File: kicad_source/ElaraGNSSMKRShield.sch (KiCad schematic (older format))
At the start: 37 parts, among them CN1 ARDUINO_MKR, CN2 60312202114509, Q1 BSS138, Q2 BSS138, U1 TPS736XX, U2 WIRL-POSI_Elara-I, U3 PCA9306, U4 SN74LVC2G34

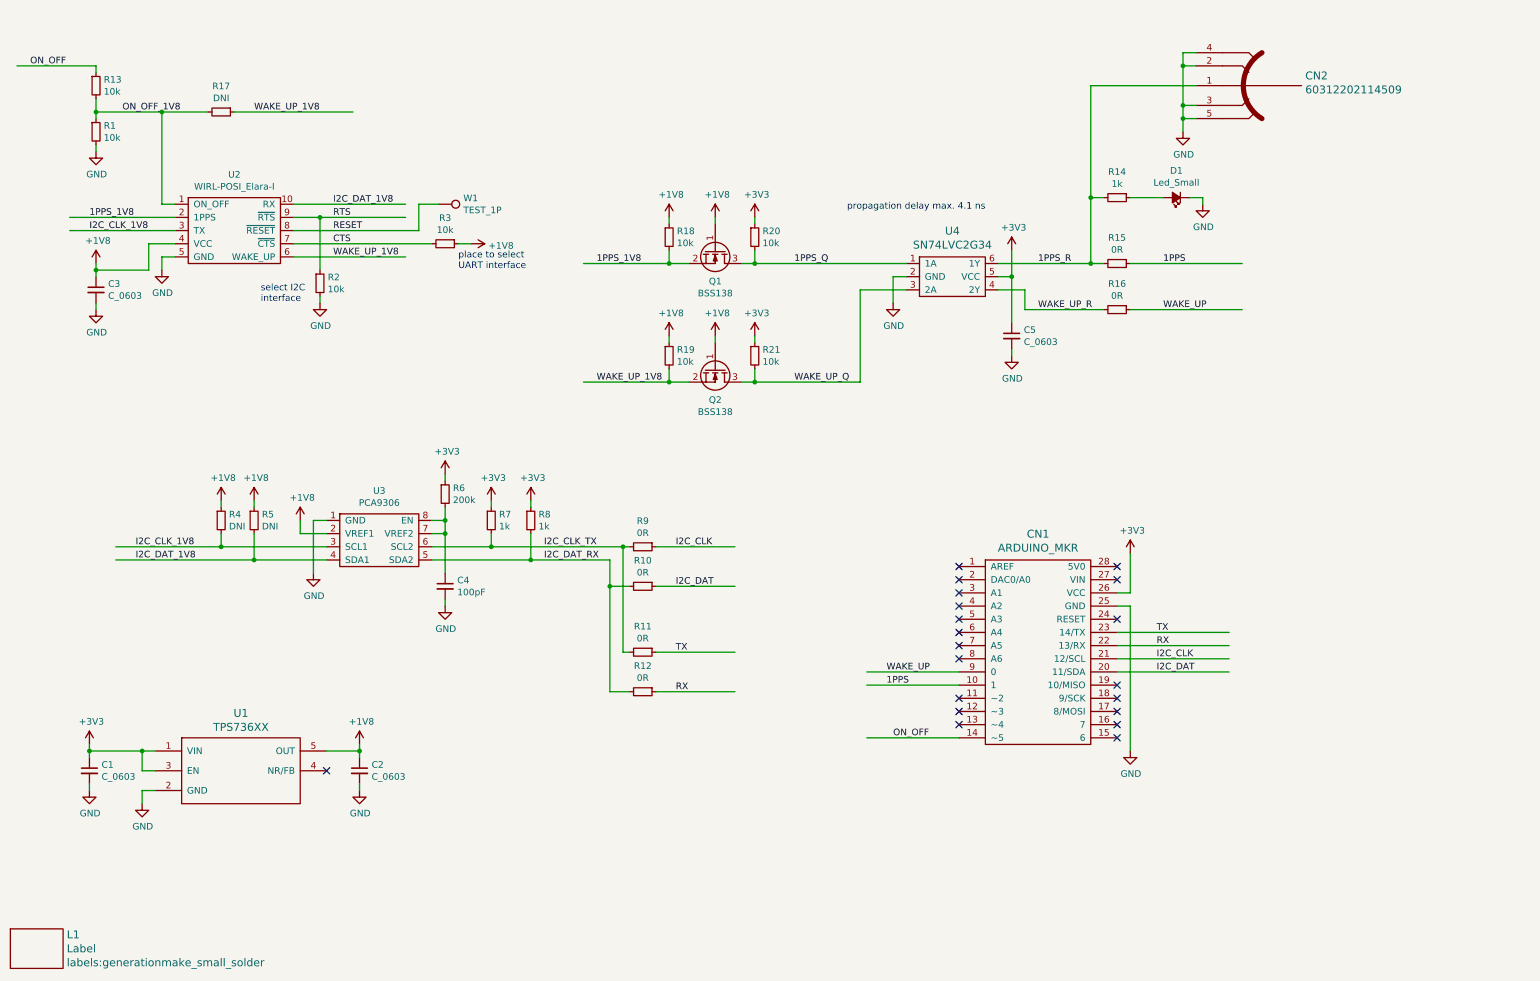
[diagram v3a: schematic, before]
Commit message: added wuerth part numbers
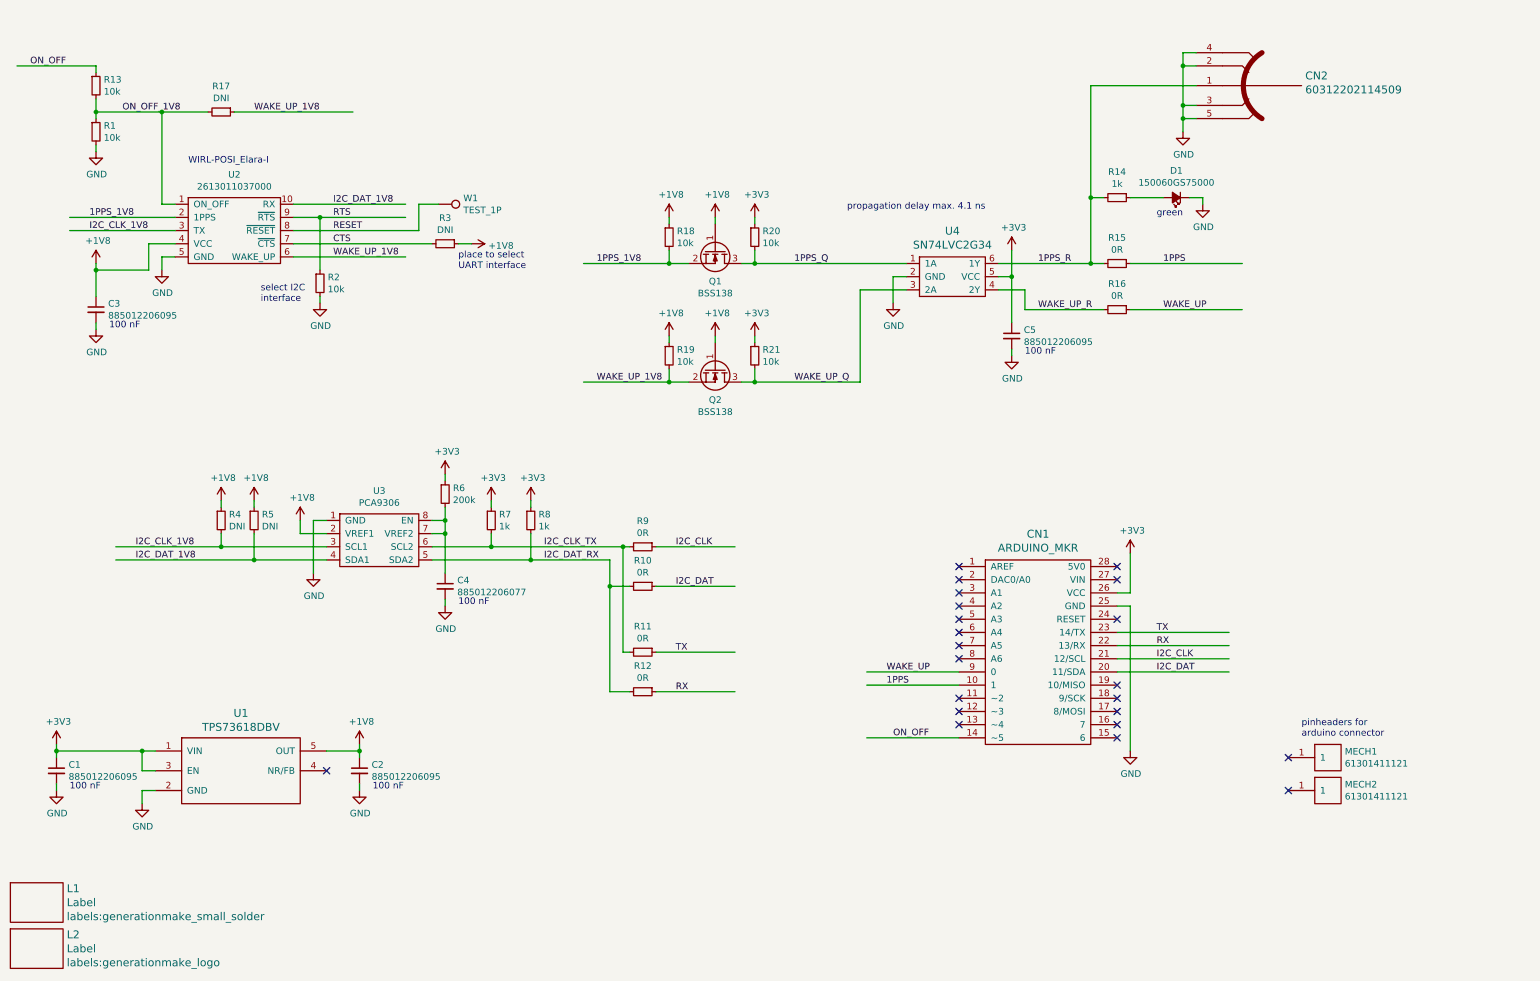
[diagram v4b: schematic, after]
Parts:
- added L2: Label, labels:generationmake_logo, symbol devices:Label
- added MECH1, MECH2: 61301411121, symbol MECH_mounting-holes:MHNP_2.1_4.0
- C1, C2, C3, C5: value C_0603 -> 885012206095
- C4: value 100pF -> 885012206077
- D1: value Led_Small -> 150060GS75000
- R3: value 10k -> DNI
- U1: value TPS736XX -> TPS73618DBV
- U2: value WIRL-POSI_Elara-I -> 2613011037000
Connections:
- no-connect marks 20 -> 22
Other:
- note added: "100 nF"
- note added: "WIRL-POSI_Elara-I"
- note added: "green"
- note added: "pinheaders for\narduino connector"
- moved on the sheet: C1, C3, L1
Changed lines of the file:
@@
 Sheet 1 1
 Title "ElaraGNSSMKRShield"
-Date "2020-11-16"
+Date "2020-12-22"
 Rev "0.1"
 Comp "generationmake"
@@
 P 2200 2150
 F 0 "U2" H 2200 2575 50  0000 C CNN
-F 1 "WIRL-POSI_Elara-I" H 2200 2484 50  0000 C CNN
+F 1 "2613011037000" H 2200 2484 50  0000 C CNN
 F 2 "RF_GPS:wuerth_WIRL-POSI_Elara-I" H 2200 2150 50  0001 C CNN
 F 3 "" H 2200 2150 50  0001 C CNN
@@
 P 2250 6200
 F 0 "U1" H 2250 6587 60  0000 C CNN
-F 1 "TPS736XX" H 2250 6481 60  0000 C CNN
+F 1 "TPS73618DBV" H 2250 6481 60  0000 C CNN
 F 2 "SOT_TO:SOT-23-5" H 2250 6350 60  0001 C CNN
 F 3 "" H 2250 6200 60  0000 C CNN
@@
 L power-supply:+3V3 #PWR01
 U 1 1 5F8A3C41
-P 1100 6050
-F 0 "#PWR01" H 1100 5900 50  0001 C CNN
-F 1 "+3V3" H 1115 6223 50  0000 C CNN
-F 2 "" H 1100 6050 50  0000 C CNN
-F 3 "" H 1100 6050 50  0000 C CNN
-	1    1100 6050
+P 850 6050
+F 0 "#PWR01" H 850 5900 50  0001 C CNN
+F 1 "+3V3" H 865 6223 50  0000 C CNN
+F 2 "" H 850 6050 50  0000 C CNN
+F 3 "" H 850 6050 50  0000 C CNN
+	1    850  6050
 	1    0    0    -1
 $EndComp
@@
 L devices:C_0603 C1
 U 1 1 5F8A5117
-P 1100 6250
-F 0 "C1" H 1192 6296 50  0000 L CNN
-F 1 "C_0603" H 1192 6205 50  0000 L CNN
-F 2 "capacitors:C_0603" H 1100 6100 50  0001 C CNN
-F 3 "" H 1100 6250 50  0000 C CNN
-	1    1100 6250
+P 850 6250
+F 0 "C1" H 942 6296 50  0000 L CNN
+F 1 "885012206095" H 942 6205 50  0000 L CNN
+F 2 "capacitors:C_0603" H 850 6100 50  0001 C CNN
+F 3 "" H 850 6250 50  0000 C CNN
+	1    850  6250
 	1    0    0    -1
 $EndComp
@@
 L power-supply:GND #PWR02
 U 1 1 5F8A62A0
-P 1100 6400
-F 0 "#PWR02" H 1100 6150 50  0001 C CNN
-F 1 "GND" H 1105 6227 50  0000 C CNN
-F 2 "" H 1100 6400 50  0000 C CNN
-F 3 "" H 1100 6400 50  0000 C CNN
-	1    1100 6400
+P 850 6400
+F 0 "#PWR02" H 850 6150 50  0001 C CNN
+F 1 "GND" H 855 6227 50  0000 C CNN
+F 2 "" H 850 6400 50  0000 C CNN
+F 3 "" H 850 6400 50  0000 C CNN
+	1    850  6400
 	1    0    0    -1
 $EndComp
@@
 P 3150 6250
 F 0 "C2" H 3242 6296 50  0000 L CNN
-F 1 "C_0603" H 3242 6205 50  0000 L CNN
+F 1 "885012206095" H 3242 6205 50  0000 L CNN
 F 2 "capacitors:C_0603" H 3150 6100 50  0001 C CNN
 F 3 "" H 3150 6250 50  0000 C CNN
@@
 	3150 6100 3150 6050
 Wire Wire Line
-	1100 6050 1100 6100
-Wire Wire Line
-	1100 6350 1100 6400
+	850  6050 850  6100
+Wire Wire Line
+	850  6350 850  6400
 Wire Wire Line
 	1600 6400 1500 6400
@@
 Wire Wire Line
 	1600 6100 1500 6100
-Connection ~ 1100 6100
-Wire Wire Line
-	1100 6100 1100 6150
+Connection ~ 850  6100
+Wire Wire Line
+	850  6100 850  6150
 Wire Wire Line
 	1600 6250 1500 6250
 Wire Wire Line
 	1500 6250 1500 6100
-Connection ~ 1500 6100
-Wire Wire Line
-	1500 6100 1100 6100
 $Comp
 L power-supply:+1V8 #PWR07
@@
 L devices:C_0603 C3
 U 1 1 5F8AB597
-P 1150 2600
-F 0 "C3" H 1242 2646 50  0000 L CNN
-F 1 "C_0603" H 1242 2555 50  0000 L CNN
-F 2 "capacitors:C_0603" H 1150 2450 50  0001 C CNN
-F 3 "" H 1150 2600 50  0000 C CNN
-	1    1150 2600
+P 1150 2750
+F 0 "C3" H 1242 2796 50  0000 L CNN
+F 1 "885012206095" H 1242 2705 50  0000 L CNN
+F 2 "capacitors:C_0603" H 1150 2600 50  0001 C CNN
+F 3 "" H 1150 2750 50  0000 C CNN
+	1    1150 2750
 	1    0    0    -1
 $EndComp
@@
 L power-supply:GND #PWR08
 U 1 1 5F8AB5A1
-P 1150 2750
-F 0 "#PWR08" H 1150 2500 50  0001 C CNN
-F 1 "GND" H 1155 2577 50  0000 C CNN
-F 2 "" H 1150 2750 50  0000 C CNN
-F 3 "" H 1150 2750 50  0000 C CNN
-	1    1150 2750
-	1    0    0    -1
-$EndComp
-Wire Wire Line
-	1150 2500 1150 2450
-Wire Wire Line
-	1150 2700 1150 2750
+P 1150 2900
+F 0 "#PWR08" H 1150 2650 50  0001 C CNN
+F 1 "GND" H 1155 2727 50  0000 C CNN
+F 2 "" H 1150 2900 50  0000 C CNN
+F 3 "" H 1150 2900 50  0000 C CNN
+	1    1150 2900
+	1    0    0    -1
+$EndComp
+Wire Wire Line
+	1150 2850 1150 2900
 Connection ~ 1150 2450
 Wire Wire Line
@@
 P 3800 2250
 F 0 "R3" V 3604 2250 50  0000 C CNN
-F 1 "10k" V 3695 2250 50  0000 C CNN
+F 1 "DNI" V 3695 2250 50  0000 C CNN
 F 2 "resistors:R_0603" H 3800 2100 50  0001 C CNN
 F 3 "" H 3800 2250 50  0000 C CNN
@@
 P 3800 4850
 F 0 "C4" H 3892 4896 50  0000 L CNN
-F 1 "100pF" H 3892 4805 50  0000 L CNN
+F 1 "885012206077" H 3892 4805 50  0000 L CNN
 F 2 "capacitors:C_0603" H 3800 4700 50  0001 C CNN
 F 3 "" H 3800 4850 50  0000 C CNN
@@
 P 8100 2950
 F 0 "C5" H 8192 2996 50  0000 L CNN
-F 1 "C_0603" H 8192 2905 50  0000 L CNN
+F 1 "885012206095" H 8192 2905 50  0000 L CNN
 F 2 "capacitors:C_0603" H 8100 2800 50  0001 C CNN
 F 3 "" H 8100 2950 50  0000 C CNN
@@
 P 9350 1900
 F 0 "D1" H 9350 1695 50  0000 C CNN
-F 1 "Led_Small" H 9350 1786 50  0000 C CNN
+F 1 "150060GS75000" H 9350 1786 50  0000 C CNN
 F 2 "LEDs:LED_0603" V 9350 1900 50  0001 C CNN
 F 3 "" V 9350 1900 50  0000 C CNN
@@
 L devices:Label L1
 U 1 1 5FB4032F
+P 700 7250
+F 0 "L1" H 928 7356 60  0000 L CNN
+F 1 "Label" H 928 7250 60  0000 L CNN
+F 2 "labels:generationmake_small_solder" H 928 7144 60  0000 L CNN
+F 3 "" H 700 7250 60  0000 C CNN
+	1    700  7250
+	1    0    0    -1
+$EndComp
+Text Notes 9200 2050 0    50   ~ 0
+green
+Text Notes 8200 3100 0    50   ~ 0
+100 nF
+Wire Wire Line
+	1150 2450 1150 2650
+Text Notes 3900 5000 0    50   ~ 0
+100 nF
+Text Notes 1250 2900 0    50   ~ 0
+100 nF
+Text Notes 950  6400 0    50   ~ 0
+100 nF
+Text Notes 3250 6400 0    50   ~ 0
+100 nF
+Wire Wire Line
+	850  6100 1500 6100
+Connection ~ 1500 6100
+Text Notes 1850 1650 0    50   ~ 0
+WIRL-POSI_Elara-I
+$Comp
+L MECH_mounting-holes:MHNP_2.1_4.0 MECH1
+U 1 1 5FE54A00
+P 10500 6150
+F 0 "MECH1" H 10628 6196 50  0000 L CNN
+F 1 "61301411121" H 10628 6105 50  0000 L CNN
+F 2 "" H 10400 6200 50  0001 C CNN
+F 3 "" H 10500 6150 50  0001 C CNN
+	1    10500 6150
+	1    0    0    -1
+$EndComp
+NoConn ~ 10200 6150
+$Comp
+L MECH_mounting-holes:MHNP_2.1_4.0 MECH2
+U 1 1 5FE5A1D3
+P 10500 6400
+F 0 "MECH2" H 10628 6446 50  0000 L CNN
+F 1 "61301411121" H 10628 6355 50  0000 L CNN
+F 2 "" H 10400 6450 50  0001 C CNN
+F 3 "" H 10500 6400 50  0001 C CNN
+	1    10500 6400
+	1    0    0    -1
+$EndComp
+NoConn ~ 10200 6400
+Text Notes 10300 6000 0    50   ~ 0
+pinheaders for\narduino connector
+$Comp
+L devices:Label L2
+U 1 1 5FE6DCD4
 P 700 7600
-F 0 "L1" H 928 7706 60  0000 L CNN
+F 0 "L2" H 928 7706 60  0000 L CNN
 F 1 "Label" H 928 7600 60  0000 L CNN
-F 2 "labels:generationmake_small_solder" H 928 7494 60  0000 L CNN
+F 2 "labels:generationmake_logo" H 928 7494 60  0000 L CNN
 F 3 "" H 700 7600 60  0000 C CNN
 	1    700  7600

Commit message: updated shape of PCB
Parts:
- added L3: Label, Symbol:OSHW-Logo_5.7x6mm_SilkScreen, symbol devices:Label
- CN1: footprint MODULE_compute:ARDUINO_MKR_HOLES_PINHEADER -> MODULE_compute:ARDUINO_MKR_HOLES_PINHEADER_EDGE
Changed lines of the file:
@@
 F 0 "CN1" H 8300 6247 60  0000 C CNN
 F 1 "ARDUINO_MKR" H 8300 6141 60  0000 C CNN
-F 2 "MODULE_compute:ARDUINO_MKR_HOLES_PINHEADER" H 8200 6000 60  0001 C CNN
+F 2 "MODULE_compute:ARDUINO_MKR_HOLES_PINHEADER_EDGE" H 8200 6000 60  0001 C CNN
 F 3 "" H 8300 5050 60  0000 C CNN
 	1    8300 5350
@@
 	1    0    0    -1
 $EndComp
+$Comp
+L devices:Label L3
+U 1 1 5FE274D4
+P 3100 7600
+F 0 "L3" H 3328 7706 60  0000 L CNN
+F 1 "Label" H 3328 7600 60  0000 L CNN
+F 2 "Symbol:OSHW-Logo_5.7x6mm_SilkScreen" H 3328 7494 60  0000 L CNN
+F 3 "" H 3100 7600 60  0000 C CNN
+	1    3100 7600
+	1    0    0    -1
+$EndComp

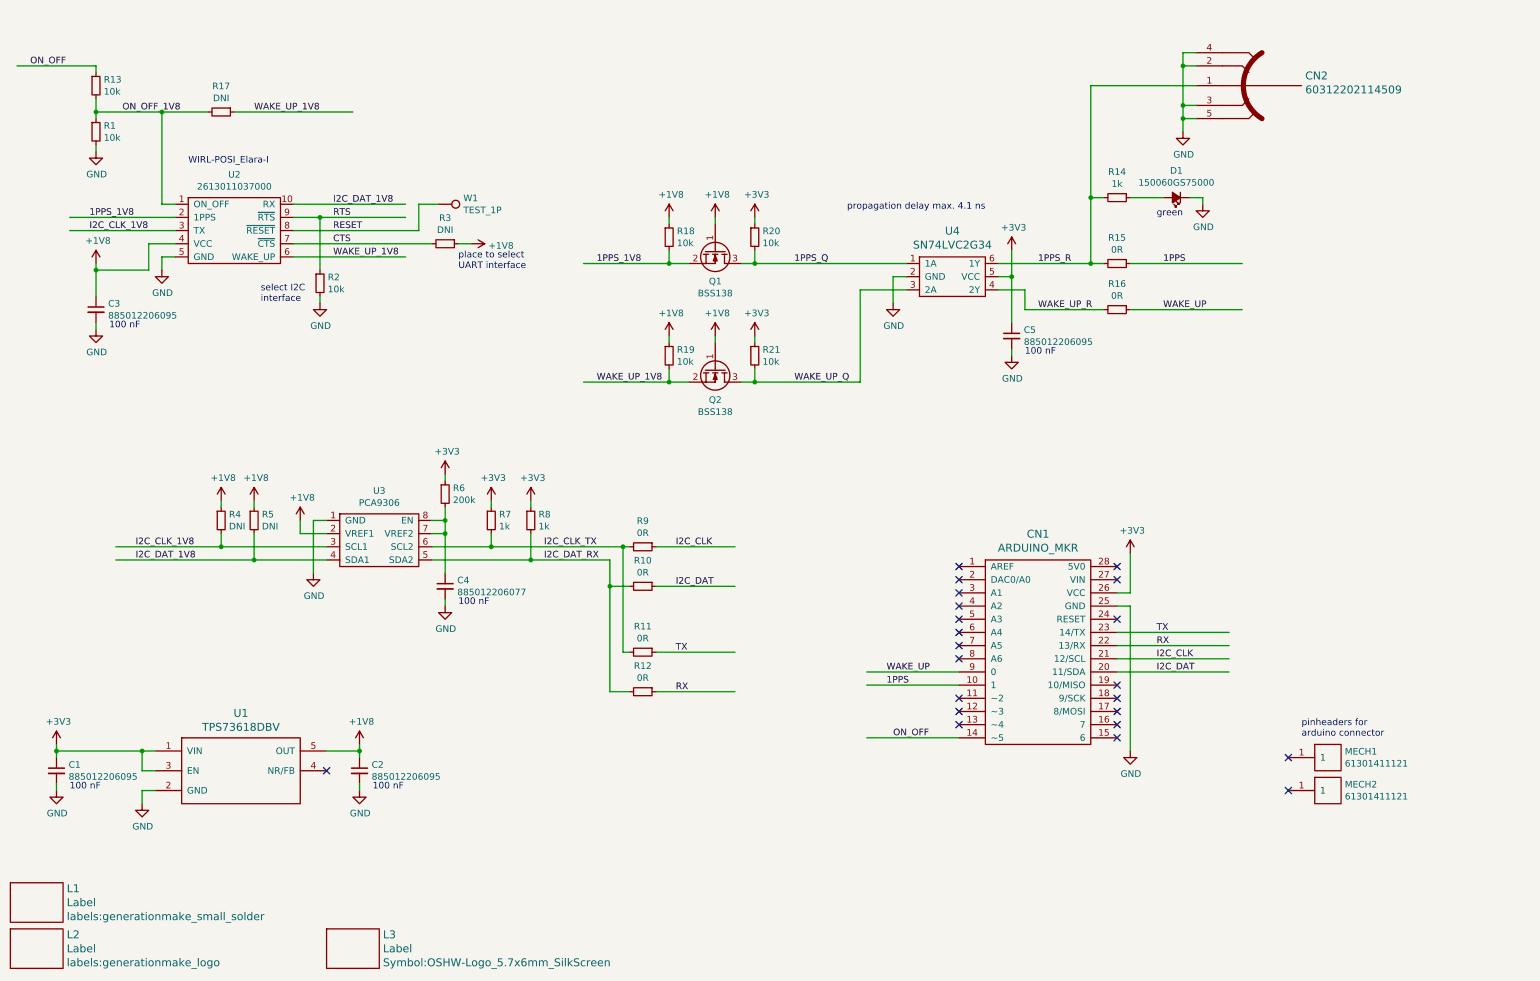
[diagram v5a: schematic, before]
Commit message: updated schematic pdf
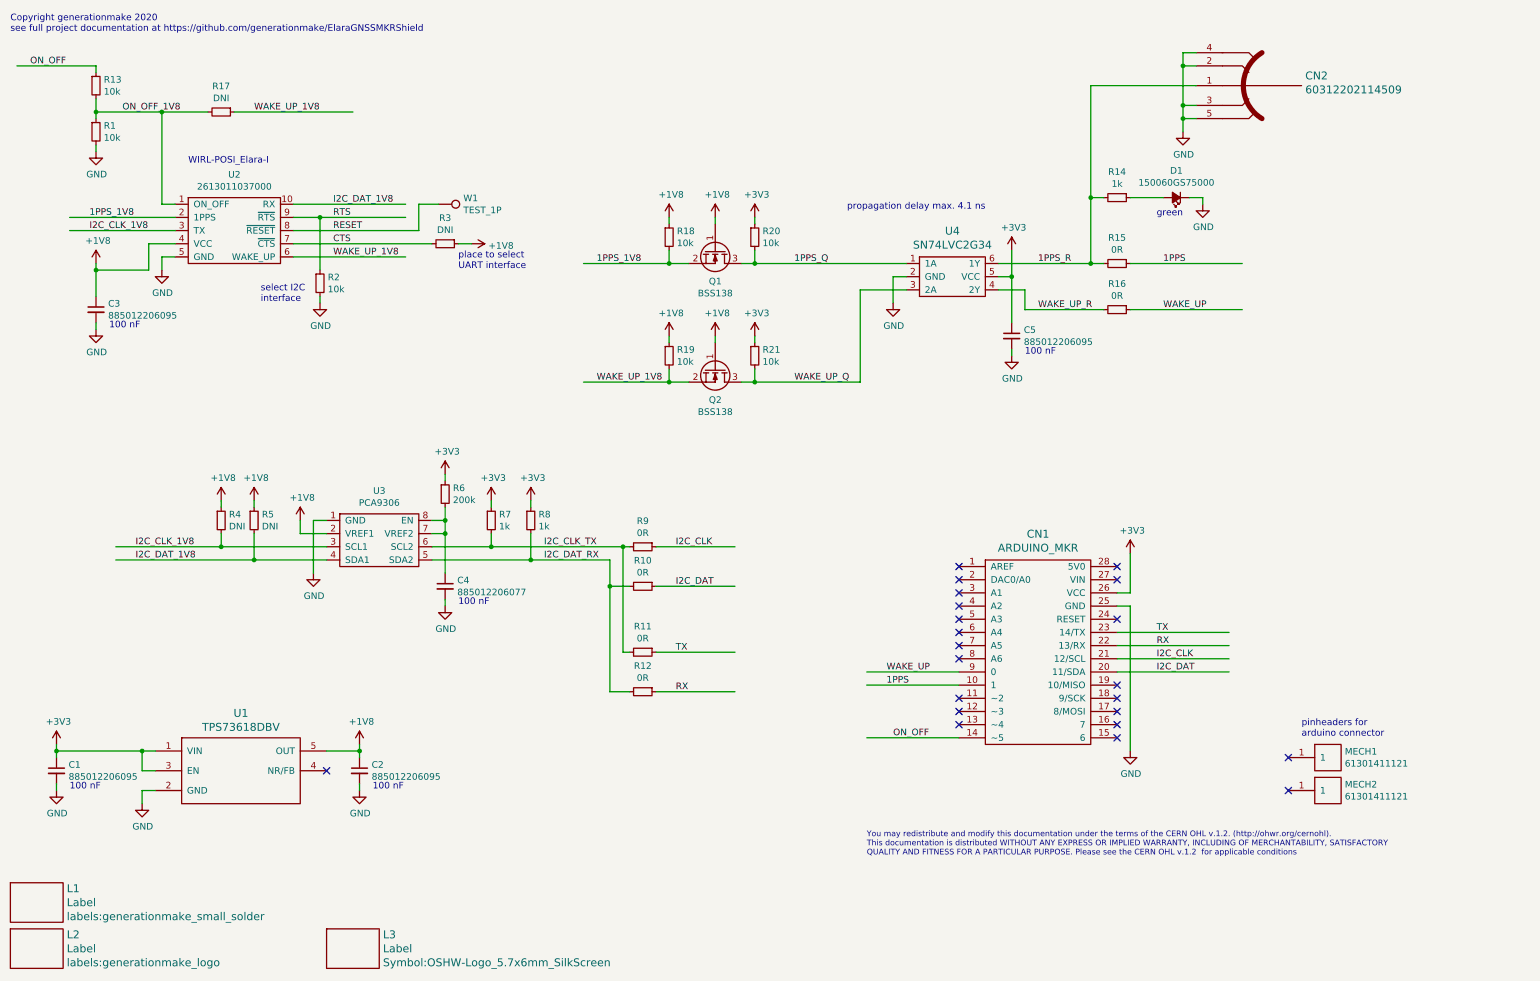
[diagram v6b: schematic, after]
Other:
- note added: "Copyright generationmake 2020\nsee full project documentation at https://github.com/generationmake/ElaraGNSSMKRShield"
- note added: "You may redistribute and modify this documentation under the terms of the CERN OHL v.1.2. (http://ohwr.org/cernohl). \nThis documentation is distributed WITHOUT ANY EXPRESS OR IMPLIED WARRANTY, INCLUDING OF MERCHANTABILITY, SATISFACTORY \nQUALITY AND FITNESS FOR A PARTICULAR PURPOSE. Please see the CERN OHL v.1.2 for applicable conditions"
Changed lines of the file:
@@
 Comment2 ""
 Comment3 ""
-Comment4 ""
+Comment4 "This documentation describes Open Hardware and is licensed under the CERN OHL v. 1.2."
 $EndDescr
 $Comp
@@
 	1    0    0    -1
 $EndComp
+Text Notes 7000 6900 0    43   ~ 0
+You may redistribute and modify this documentation under the terms of the CERN OHL v.1.2. (http://ohwr.org/cernohl). \nThis documentation is distributed WITHOUT ANY EXPRESS OR IMPLIED WARRANTY, INCLUDING OF MERCHANTABILITY, SATISFACTORY \nQUALITY AND FITNESS FOR A PARTICULAR PURPOSE. Please see the CERN OHL v.1.2  for applicable conditions
+Text Notes 500  650  0    50   ~ 0
+Copyright generationmake 2020\nsee full project documentation at https://github.com/generationmake/ElaraGNSSMKRShield
 $EndSCHEMATC
